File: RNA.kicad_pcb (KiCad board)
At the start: 2 copper layers, 134 x 177 mm, 164 parts, among them J1 USB_B_Micro, J2 AudioJack4, J3 AudioJack4, J4 Conn_01x06, J5 AudioJack4, SW1 SW_SPST, SW10 CPG135001S30, SW11 CPG135001S30, SW12 CPG135001S30, SW13 CPG135001S30, SW14 CPG135001S30, SW15 CPG135001S30, SW16 CPG135001S30, SW17 CPG135001S30, SW18 CPG135001S30, SW19 CPG135001S30, SW2 SW_Push, SW20 CPG135001S30, SW21 CPG135001S30, SW22 CPG135001S30, SW23 CPG135001S30, SW24 CPG135001S30, SW25 CPG135001S30, SW26 CPG135001S30, SW27 CPG135001S30, SW28 CPG135001S30, SW29 CPG135001S30, SW3 CPG135001S30, SW30 CPG135001S30, SW31 CPG135001S30, SW32 CPG135001S30, SW33 CPG135001S30, SW34 CPG135001S30, SW35 CPG135001S30, SW36 CPG135001S30, SW37 CPG135001S30, SW38 CPG135001S30, SW39 CPG135001S30, SW4 CPG135001S30, SW40 CPG135001S30, SW41 CPG135001S30, SW42 CPG135001S30, SW43 CPG135001S30, SW44 CPG135001S30, SW45 CPG135001S30, SW46 CPG135001S30, SW47 CPG135001S30, SW48 CPG135001S30, SW49 CPG135001S30, SW5 CPG135001S30, SW50 CPG135001S30, SW51 CPG135001S30, SW52 CPG135001S30, SW53 CPG135001S30, SW54 CPG135001S30, SW55 CPG135001S30, SW56 CPG135001S30, SW57 CPG135001S30, SW58 CPG135001S30, SW59 CPG135001S30, SW6 CPG135001S30, SW60 CPG135001S30, SW61 CPG135001S30, SW62 CPG135001S30, SW63 CPG135001S30, SW64 CPG135001S30, SW65 CPG135001S30, SW66 CPG135001S30, SW7 CPG135001S30, SW8 CPG135001S30, SW9 CPG135001S30, U1 STM32F072C8Tx, U2 PRTR5V0U2X, U3 MCP1703A-3302_SOT23, U4 CAT24M01W, U5 MCP23017_SS

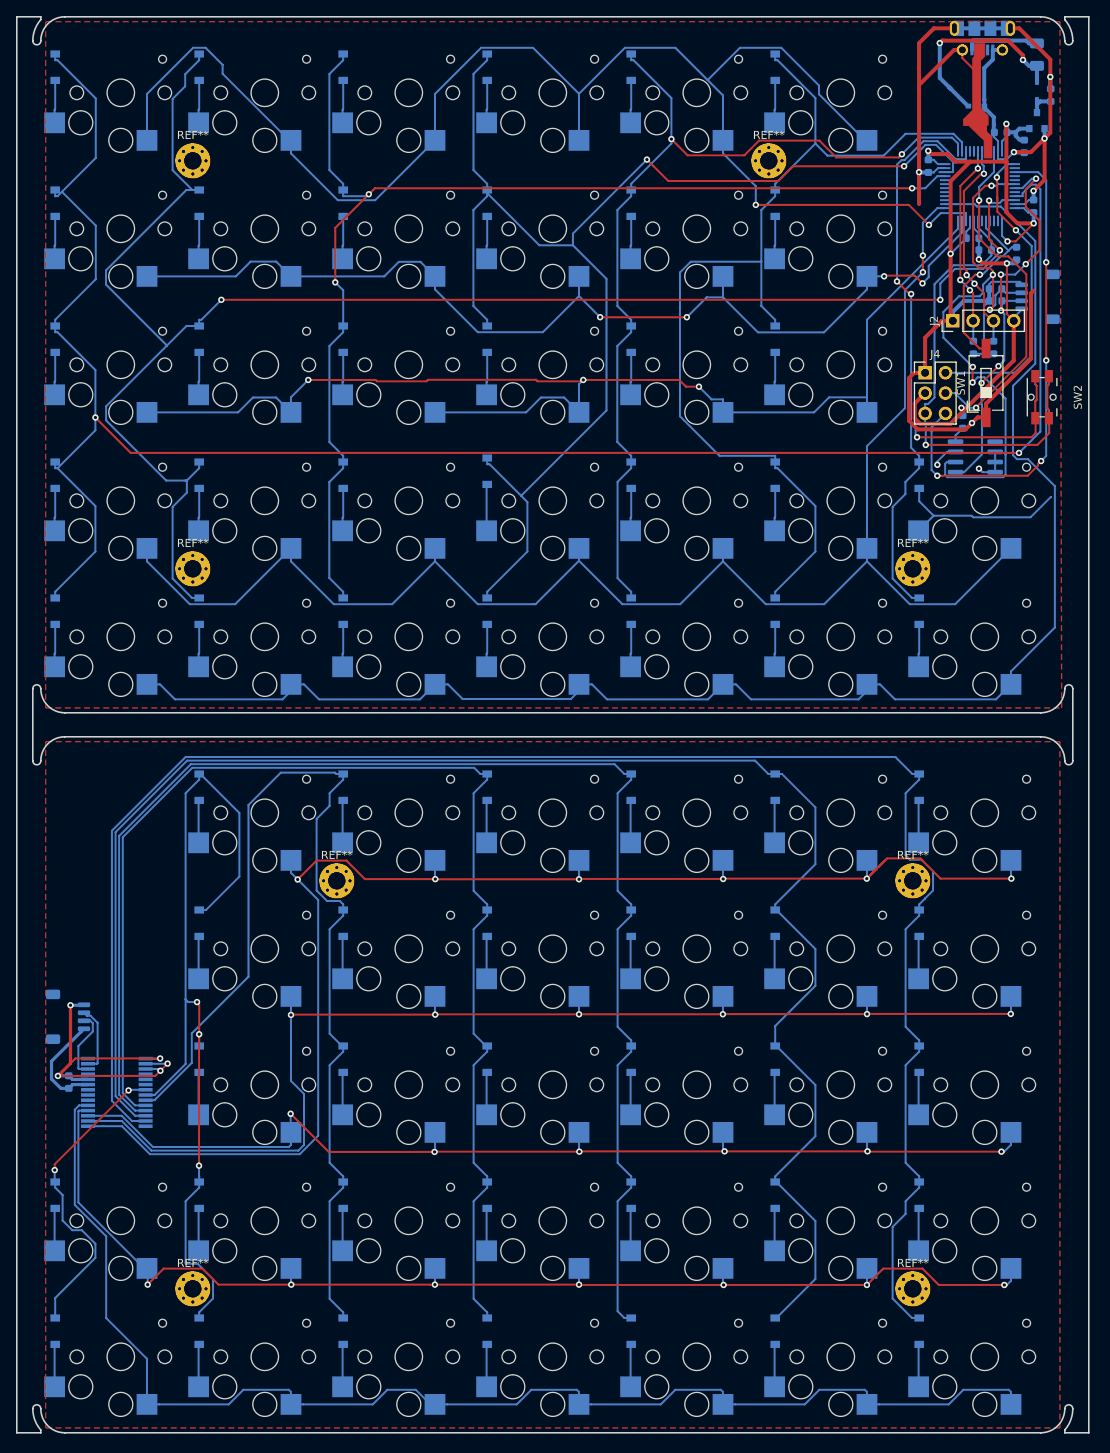
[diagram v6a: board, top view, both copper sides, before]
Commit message: arrange reference footprint
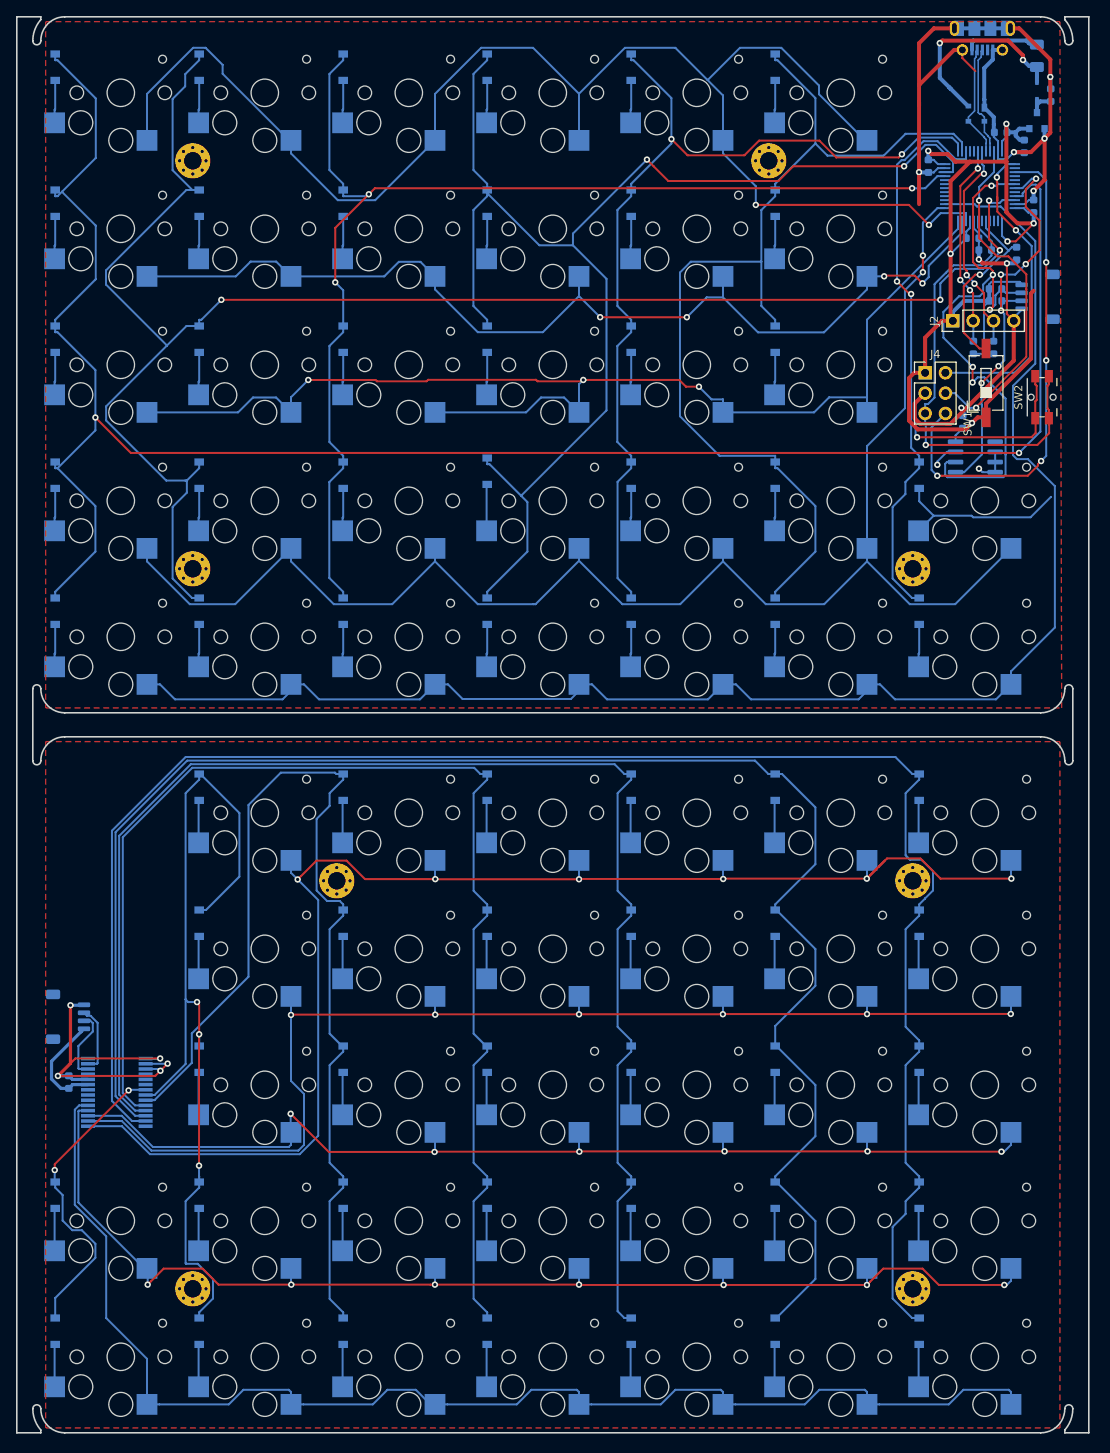
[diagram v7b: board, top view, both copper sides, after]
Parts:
- moved F1 0.15 mm to (143.5, 23.9)

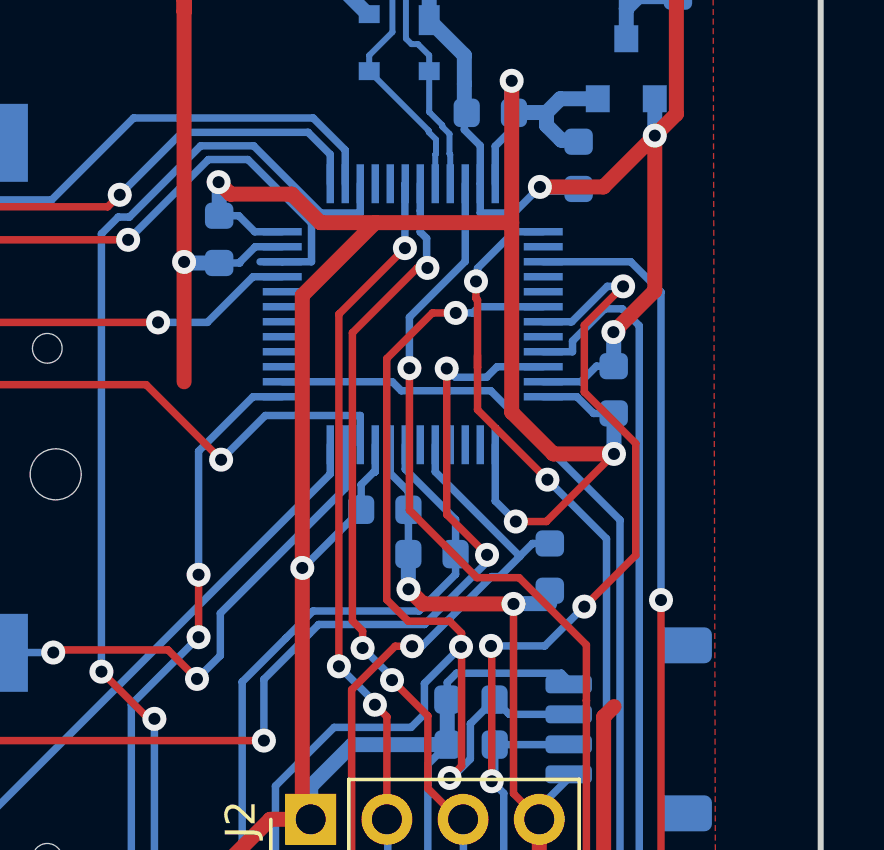
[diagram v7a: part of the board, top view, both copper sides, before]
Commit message: Move conflicted I2C1 to I2C3
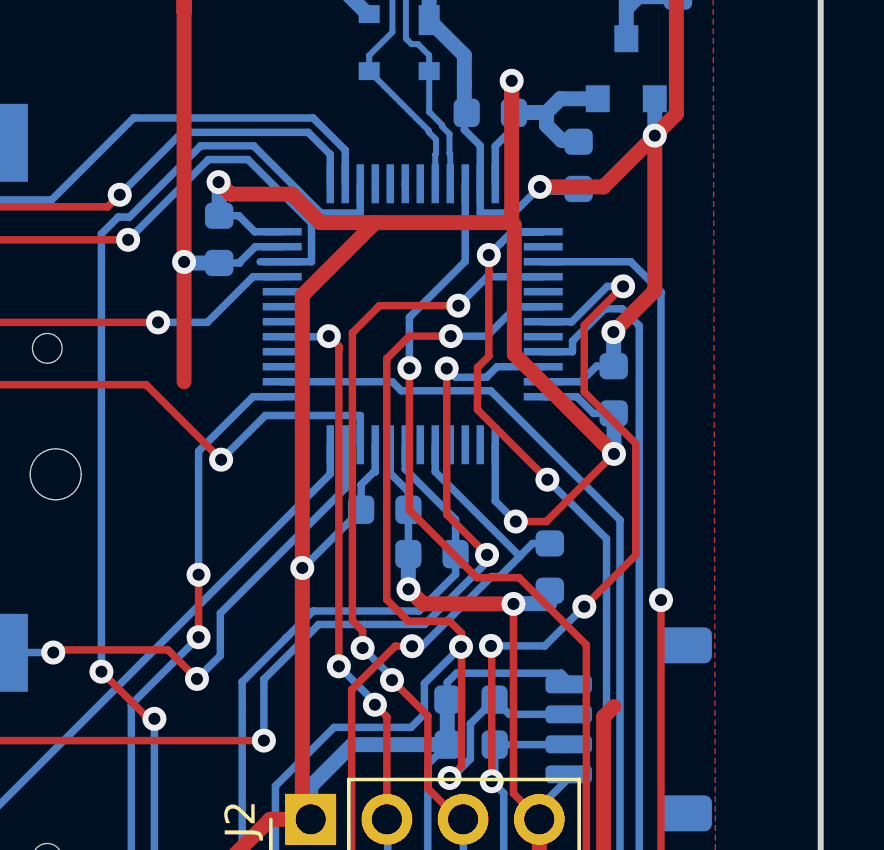
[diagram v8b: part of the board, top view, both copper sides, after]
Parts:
- J2, J5: value AudioJack4 -> SM04B-SRSS-TB(LF)(SN)
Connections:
- J2 pad 2: SCL2 -> SCL3
- J2 pad 3: SDA2 -> SDA3
- R2 pad 2: SDA2 -> SDA3
- R3 pad 2: SCL2 -> SCL3
- U1 pad 17: Net-(U1-Pad17) -> SCL3
- U1 pad 30: SCL2 -> Net-(U1-Pad30)
- U1 pad 31: SDA2 -> Net-(U1-Pad31)
- U1 pad 40: Net-(U1-Pad40) -> SDA3
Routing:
- net SDA3: track 0.00 -> 27.5 mm, vias 0 -> 3
- net SDA2: track 26.7 -> 0.00 mm, vias 3 -> 0
- net SCL2: track 25.3 -> 0.00 mm, vias 3 -> 0
- net SCL3: track 0.00 -> 21.0 mm, vias 0 -> 3
- net VDD: track 159.6 -> 158.4 mm
- net SWCLK: track 39.3 -> 39.9 mm
